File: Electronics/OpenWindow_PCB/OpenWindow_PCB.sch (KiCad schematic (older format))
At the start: 29 parts

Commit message: Initial PCB layout
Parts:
- removed D?: 1N4007, Diode_THT:D_DO-41_SOD81_P10.16mm_Horizontal, symbol Diode:1N4007
- removed J?: Door connector, symbol Connector_Generic:Conn_01x05
- removed J?: EFM8 EXP0, symbol Connector_Generic:Conn_02x10_Odd_Even
- removed K? (x2): MCCMA31-DC12V-C, Connector_PinHeader_1.00mm:PinHeader_1x05_P1.00mm_Horizontal, symbol OpenWindow:MCCMA31-DC12V-C
- removed M?: Motor_DC, symbol Motor:Motor_DC
- removed Q?: PN2222A, Package_TO_SOT_THT:TO-92_Inline, symbol Transistor_BJT:PN2222A
- removed R?: 1K, symbol Device:R
- removed U?: ACS712_PCB, symbol OpenWindow:ACS712_PCB
- added C1, C5: 100n, Capacitor_SMD:C_0805_2012Metric_Pad1.18x1.45mm_HandSolder, symbol Device:C
- added C6: 1uF, Capacitor_THT:CP_Radial_D5.0mm_P2.00mm, symbol Device:CP
- added C7: 4.7u, Capacitor_SMD:C_0805_2012Metric_Pad1.18x1.45mm_HandSolder, symbol Device:C
- added C8: 2.2uF, Capacitor_THT:CP_Radial_D5.0mm_P2.00mm, symbol Device:CP
- added D2: LED, LED_THT:LED_D3.0mm, symbol Device:LED
- added D4: 1N4007, Diode_THT:D_DO-41_SOD81_P10.16mm_Horizontal, symbol Diode:1N4007
- added J1: Door connector, Connector_JST:JST_XH_B4B-XH-AM_1x04_P2.50mm_Vertical, symbol Connector_Generic:Conn_01x04
- added J2: C2 connector, Connector_PinHeader_2.54mm:PinHeader_1x03_P2.54mm_Vertical, symbol Connector_Generic:Conn_01x03
- added J3: FTDI connector, Connector_PinHeader_2.54mm:PinHeader_1x06_P2.54mm_Vertical, symbol Connector_Generic:Conn_01x06
- added J4: Relay Connector 2, TerminalBlock_Phoenix:TerminalBlock_Phoenix_MKDS-3-2-5.08_1x02_P5.08mm_Horizontal, symbol Connector_Generic:Conn_01x02
- added J5: ACS712 PCB Connector, Connector_JST:JST_XH_B3B-XH-A_1x03_P2.50mm_Vertical, symbol Connector_Generic:Conn_01x03
- added J6: Relay Connector 1, TerminalBlock_Phoenix:TerminalBlock_Phoenix_MKDS-3-2-5.08_1x02_P5.08mm_Horizontal, symbol Connector_Generic:Conn_01x02
- added Q5: PN2222A, Package_TO_SOT_THT:TO-92_Inline, symbol Transistor_BJT:PN2222A
- added R1, R2: 1K, Resistor_SMD:R_0603_1608Metric_Pad0.98x0.95mm_HandSolder, symbol Device:R
- added R11: 1K6, Resistor_THT:R_Axial_DIN0411_L9.9mm_D3.6mm_P12.70mm_Horizontal, symbol Device:R
- added R13: 1K, Resistor_THT:R_Axial_DIN0411_L9.9mm_D3.6mm_P12.70mm_Horizontal, symbol Device:R
- added R3: 100R, Resistor_SMD:R_0603_1608Metric_Pad0.98x0.95mm_HandSolder, symbol Device:R
- added SW1: SW_Push, Button_Switch_THT:SW_PUSH_6mm, symbol Switch:SW_Push
- added U2: LP2950-3.3_TO92, Package_TO_SOT_THT:TO-92_Inline, symbol Regulator_Linear:LP2950-3.3_TO92
- added U3: EFM8BB21F16I-C-QSOP24, Package_SO:QSOP-24_3.9x8.7mm_P0.635mm, symbol OpenWindow:EFM8BB21F16I-C-QSOP24
- C2: renamed from C?; value 2.2uF -> 1uF; footprint (none) -> Capacitor_THT:CP_Radial_D5.0mm_P2.00mm
- C3, C4: renamed from C?; footprint (none) -> Capacitor_THT:CP_Radial_D5.0mm_P2.00mm
- R10, R12, R14, R15, R4, R5, R6, R7, R8, R9: renamed from R?; footprint (none) -> Resistor_THT:R_Axial_DIN0411_L9.9mm_D3.6mm_P12.70mm_Horizontal
- gave numbers to parts that had none: 7
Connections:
- net +12V: now also J1.2 (Pin_2)
- net +12V_switched: now also C6.1, D4.1 (K), J4.1 (Pin_1), J6.1 (Pin_1), U2.3 (VI)
- net +5V: now also J5.1 (Pin_1)
- net ADC_in: now also U3.21 (P0.7)
- net CMP0_in: now also U3.19 (P1.1), U3.4 (P0.0)
- net GND: now also C1.2, C5.2, C6.2, C7.2, C8.2, D2.1 (K), J1.1 (Pin_1), J2.3 (Pin_3), J3.1 (Pin_1), J5.3 (Pin_3), Q5.1 (E), R3.1, U2.2 (GND), U3.5 (GND)
- net Motor_GPIO_1: now also R12.2, U3.10 (P2.2)
- net Motor_GPIO_2: now also R13.2, U3.11 (P2.1); no longer R12.2
- net at D3.2 (A), Q4.3 (C): now also J4.2 (Pin_2)
- net at R15.1: now also J5.2 (Pin_2)
- net Ignition_input renamed Ignition_in
- net Ignition_in: now also J1.3 (Pin_3)
- net Switch_input renamed WindowSwitch_in
- net WindowSwitch_in: now also J1.4 (Pin_4)
- new net: D2.2 (A), R11.1
- new net: C1.1, R1.1, R2.1, SW1.1
- new net: R3.2, SW1.2
- new net: Q5.2 (B), R13.1
- new net: D4.2 (A), J6.2 (Pin_2), Q5.3 (C)
- new net +3V3: C5.1, C7.1, C8.1, R11.2, R2.2, U2.1 (VO), U3.6 (VDD)
- new net C2CK: J2.1 (Pin_1), R1.2, U3.7 (RSTn/C2CK)
- new net C2D: J2.2 (Pin_2), U3.8 (P3.0/C2D)
- new net UART1_RX: J3.4 (Pin_4), U3.23 (P0.5)
- new net UART1_TX: J3.5 (Pin_5), U3.24 (P0.4)
- no-connect marks 15 -> 16
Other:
- note added: "3V3 supply"
- note added: "C2 debug"
- note added: "FTDI serial"
- note added: "Reset button"
- note added: "Supply protection"
- note added: "Window switch comparator"
- note removed: "EMF8BB2 Dev Board\n"
- note removed: "Input protection"
- note removed: "Switch comparator"
- moved on the sheet: C2, C3, C4, D1, D3, Q1, Q2, Q3, Q4, R10, R12, R14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

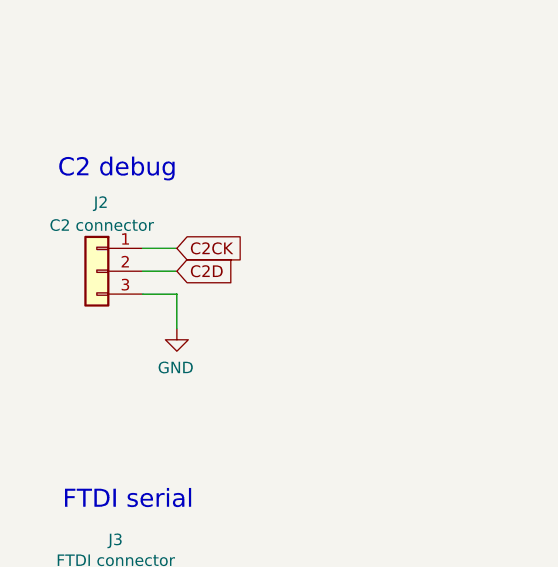
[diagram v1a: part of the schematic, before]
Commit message: Corrected C2 debug header
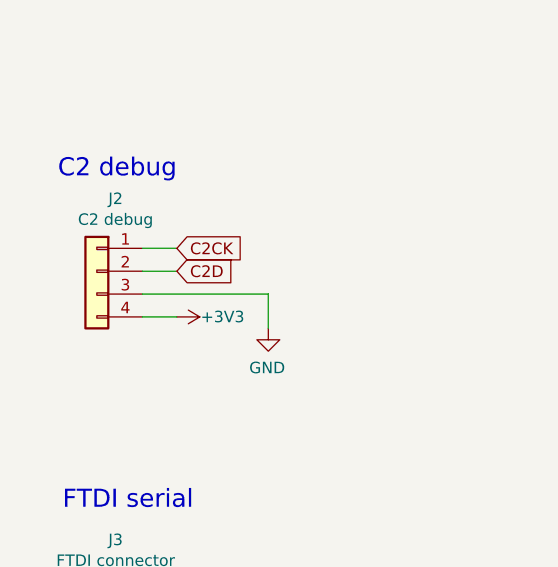
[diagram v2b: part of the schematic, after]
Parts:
- removed J2: C2 connector, Connector_PinHeader_2.54mm:PinHeader_1x03_P2.54mm_Vertical, symbol Connector_Generic:Conn_01x03
- added J2: C2 debug, Connector_PinHeader_2.54mm:PinHeader_1x04_P2.54mm_Vertical, symbol Connector_Generic:Conn_01x04
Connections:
- net +3V3: now also J2.4 (Pin_4)
- net C2CK: now also J2.1 (Pin_1)
- net C2D: now also J2.2 (Pin_2)
- net GND: now also J2.3 (Pin_3)
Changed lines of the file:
@@
 Connection ~ 8300 4700
-$Comp
-L Connector_Generic:Conn_01x03 J2
-U 1 1 6024B9BE
-P 1050 3000
-F 0 "J2" H 1000 3300 50  0000 L CNN
-F 1 "C2 connector" H 800 3200 50  0000 L CNN
-F 2 "Connector_PinHeader_2.54mm:PinHeader_1x03_P2.54mm_Vertical" H 1050 3000 50  0001 C CNN
-F 3 "~" H 1050 3000 50  0001 C CNN
-	1    1050 3000
-	-1   0    0    -1
-$EndComp
 $Comp
 L power:GND #PWR02
 U 1 1 6025AAA8
-P 1400 3250
-F 0 "#PWR02" H 1400 3000 50  0001 C CNN
-F 1 "GND" H 1405 3077 50  0000 C CNN
-F 2 "" H 1400 3250 50  0001 C CNN
-F 3 "" H 1400 3250 50  0001 C CNN
-	1    1400 3250
+P 1800 3250
+F 0 "#PWR02" H 1800 3000 50  0001 C CNN
+F 1 "GND" H 1805 3077 50  0000 C CNN
+F 2 "" H 1800 3250 50  0001 C CNN
+F 3 "" H 1800 3250 50  0001 C CNN
+	1    1800 3250
 	-1   0    0    -1
 $EndComp
-Wire Wire Line
-	1250 3100 1400 3100
-Wire Wire Line
-	1400 3100 1400 3250
 Text Notes 1400 2600 2    79   ~ 0
 C2 debug
@@
 Wire Wire Line
 	7000 2950 7000 3050
+$Comp
+L Connector_Generic:Conn_01x04 J2
+U 1 1 60585D2A
+P 1050 3000
+F 0 "J2" H 968 3317 50  0000 C CNN
+F 1 "C2 debug" H 968 3226 50  0000 C CNN
+F 2 "Connector_PinHeader_2.54mm:PinHeader_1x04_P2.54mm_Vertical" H 1050 3000 50  0001 C CNN
+F 3 "~" H 1050 3000 50  0001 C CNN
+	1    1050 3000
+	-1   0    0    -1
+$EndComp
+Wire Wire Line
+	1800 3100 1800 3250
+$Comp
+L power:+3V3 #PWR0101
+U 1 1 60599B75
+P 1400 3200
+F 0 "#PWR0101" H 1400 3050 50  0001 C CNN
+F 1 "+3V3" V 1400 3400 50  0000 C CNN
+F 2 "" H 1400 3200 50  0001 C CNN
+F 3 "" H 1400 3200 50  0001 C CNN
+	1    1400 3200
+	0    1    1    0
+$EndComp
+Wire Wire Line
+	1250 3200 1400 3200
+Wire Wire Line
+	1250 3100 1800 3100
 $EndSCHEMATC
